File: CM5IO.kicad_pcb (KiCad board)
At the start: 8 copper layers, 130 x 80 mm, 62 parts, among them J1 Conn_02x06_Top_Bottom, J14 JST_SHBM04B-SRSS-TB, J16 Conn_01x22_Female, J22 690-019-298-412, J3 Conn_01x03, J4 Bus_M.2_Socket_M, J6 THD-02-R, U1 TPD4EUSB30, U12 RT9742SNGV, U2 TPD4EUSB30, U5 74LVC1G07SE-7, U6 AP22653W6, U7 ASEK-32.768KHZ-L-R-T, U8 AP3441SHE-7B

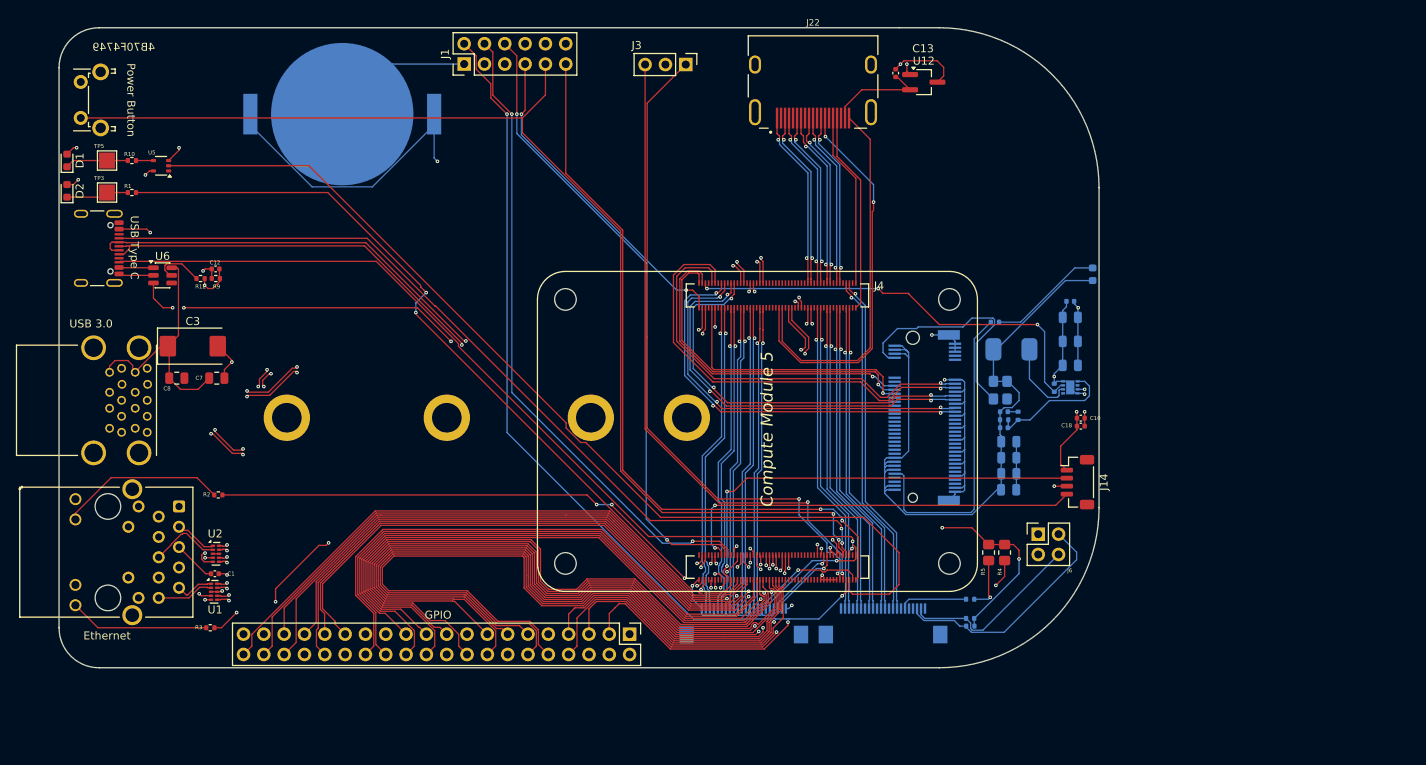
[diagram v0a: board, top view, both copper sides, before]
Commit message: Added model for Fan connector (JST_SH_BM04B-SRSS-TB_1x04-1MP_P1.00mm_Vertical) Thickened power and voltage lines Tuned all high speed lines for skew
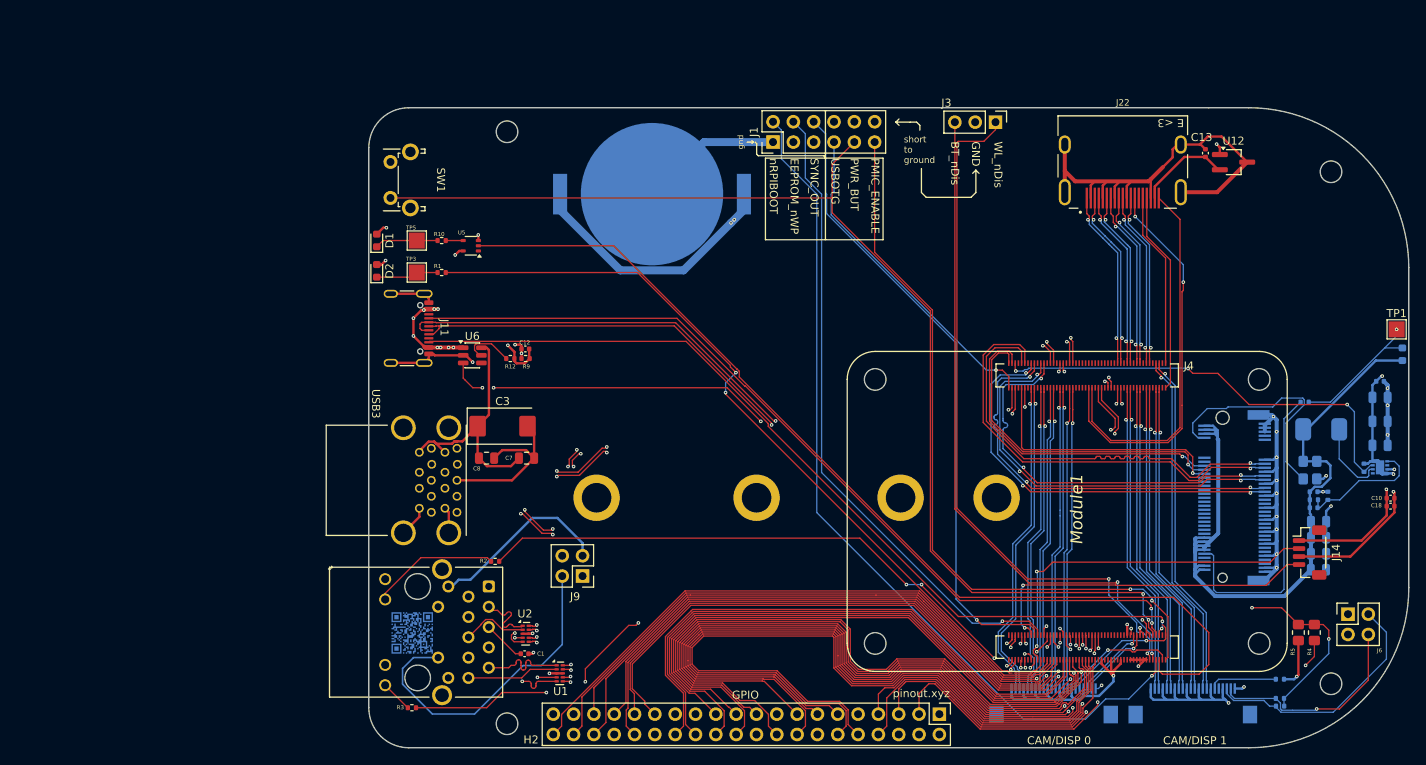
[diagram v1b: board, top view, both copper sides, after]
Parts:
- added H1: MountingHole, CM5IO:MountingHole_2.7mm_M2.5_DIN965, F.Cu at (106.0, 63.0)
- added H2: MountingHole, CM5IO:MountingHole_2.7mm_M2.5_DIN965, F.Cu at (106.0, 137.0)
- added H3: MountingHole, CM5IO:MountingHole_2.7mm_M2.5_DIN965, F.Cu at (209.0, 68.0)
- added H4: MountingHole, CM5IO:MountingHole_2.7mm_M2.5_DIN965, F.Cu at (209.0, 132.0)
- added J9: THD-02-R, Connector_PinHeader_2.54mm:PinHeader_2x02_P2.54mm_Vertical, F.Cu at (115.4, 118.5)
- added TP1: TestPoint, TestPoint:TestPoint_Pad_2.0x2.0mm, F.Cu at (217.2, 87.7)
- J11: renamed from USB Type C
- Module1: renamed from Compute Module 5
- SW1: renamed from Power Button
- USB3: renamed from USB 3.0
- moved U1 44.4 mm to (112.6, 130.7)
- moved R15 40.0 mm to (206.9, 109.0)
- moved R6 40.0 mm to (202.6, 133.8)
- moved R8 40.0 mm to (202.6, 131.4)
- moved C12 40.0 mm to (108.3, 90.2)
- moved R9 40.0 mm to (108.3, 91.3)
- moved SW1 40.0 mm to (91.4, 71.3)
- moved USB3 40.0 mm to (93.0, 106.6)
- moved BT1 40.0 mm to (124.1, 70.8)
- moved C1 40.0 mm to (108.2, 128.2)
- moved C10 40.0 mm to (216.4, 108.8)
- moved C11 40.0 mm to (206.8, 110.0)
- moved C13 40.0 mm to (193.3, 65.7)
- moved C14 40.0 mm to (207.4, 117.8)
- moved C15 40.0 mm to (207.4, 115.8)
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- renumbered MIPI to J5
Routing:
- net GND: track 130.7 -> 295.5 mm, vias 13 -> 23
- net /CM5_GPIO ( Ethernet, GPIO, SDCARD)/TR1_TAP: track 0.00 -> 73.4 mm
- net /CM5_GPIO ( Ethernet, GPIO, SDCARD)/TR3_TAP: track 0.00 -> 47.3 mm
- net /CM5_GPIO ( Ethernet, GPIO, SDCARD)/TR2_TAP: track 0.00 -> 40.6 mm
- net /CM5_GPIO ( Ethernet, GPIO, SDCARD)/TR0_TAP: track 0.00 -> 23.3 mm
- net Net-(U3-LEDG_K): track 17.5 -> 3.98 mm
- net /CM5_GPIO ( Ethernet, GPIO, SDCARD)/ETH_LEDY: track 66.7 -> 80.2 mm
- net /+5v: track 32.5 -> 44.6 mm, vias 7 -> 18
- net /CM5_GPIO ( Ethernet, GPIO, SDCARD)/PWM: track 54.7 -> 45.5 mm
- net /CM5_GPIO ( Ethernet, GPIO, SDCARD)/TACHO: track 51.7 -> 42.7 mm
- net /CM5_GPIO ( Ethernet, GPIO, SDCARD)/ETH_LEDG: track 68.5 -> 75.8 mm
- net /PCIe-M2/M2_3v3: track 87.1 -> 92.2 mm
- net Net-(U3-LEDY_K): track 20.9 -> 16.0 mm
- net /CM5_GPIO ( Ethernet, GPIO, SDCARD)/WL_nDis: track 83.0 -> 87.7 mm
- net /CM5_HighSpeed/USB3-0-D_N: track 114.6 -> 118.3 mm
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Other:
- board text added: "BT_nDis"
- board text added: "Battery: CR2032"
- board text added: "CAM/DISP 0"
- board text added: "CAM/DISP 1"
- board text added: "Doruk Kaya ${PROJ_TIME_DD}/${PROJ_TIME_MM}/${PROJ_TIME_YYYY} v${PROJ_REV_MAJOR}.${PROJ_REV_MINOR}"
- board text added: "EEPROM_nWP"
- board text added: "GND"
- board text added: "PMIC_ENABLE"
- board text added: "PWR_BUT"
- board text added: "SYNC_OUT"
- board text added: "USBOTG"
- board text added: "WL_nDis"
- board text added: "board id: ${PROJ_TIME_YYYY}${PROJ_TIME_MM}${PROJ_ID}${PROJ_REV_MAJOR}${PROJ_REV_MINOR}"
- board text added: "gnd"
- board text added: "nRPIBOOT"
- board text added: "pinout.xyz"
- board text added: "short to ground"
- board text removed: "4B70F4749"
- board text removed: "Doruk Kaya 23/11/2025 v0.01"
